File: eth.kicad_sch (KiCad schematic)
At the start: 34 parts

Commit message: add USB
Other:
- company: (none) -> M-Labs
- title: (none) -> Kirdy
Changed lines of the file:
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@@
 (kicad_sch (version 20211123) (generator eeschema)
   (paper "A3")
+  (title_block
+    (title "Kirdy")
+    (date "2022-07-03")
+    (rev "r0.1")
+    (company "M-Labs")
+    (comment 1 "Alex Wong Tat Hang")
+  )
   (junction (at 191.77 163.83) (diameter 0) (color 0 0 0 0)
   )

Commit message: complete mcu
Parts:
- gave numbers to parts that had none: 34

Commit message: first draft complete
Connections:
- net +3V3: now also C166.1, U26.9 (VDDIO)
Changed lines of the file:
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@@
     (pin "2")
+  )
+  (symbol (lib_id "power:+3V3") (at 191.77 151.13 0) (unit 1)
+    (in_bom yes) (on_board yes)
+    (property "Reference" "#PWR0161" (id 0) (at 191.77 154.94 0)
+      (effects (font (size 1.27 1.27)) hide)
+    )
+    (property "Value" "+3V3" (id 1) (at 191.77 147.32 0))
+    (property "Footprint" "" (id 2) (at 191.77 151.13 0)
+      (effects (font (size 1.27 1.27)) hide)
+    )
+    (property "Datasheet" "" (id 3) (at 191.77 151.13 0)
+      (effects (font (size 1.27 1.27)) hide)
+    )
+    (pin "1")
   )
   (symbol (lib_id "Device:R") (at 300.99 128.27 90) (unit 1)
@@
     (pin "2")
   )
+  (symbol (lib_id "power:PWR_FLAG") (at 204.47 146.05 0) (unit 1)
+    (in_bom yes) (on_board yes) (fields_autoplaced)
+    (property "Reference" "#FLG0117" (id 0) (at 204.47 144.145 0)
+      (effects (font (size 1.27 1.27)) hide)
+    )
+    (property "Value" "PWR_FLAG" (id 1) (at 204.47 140.97 0)
+      (effects (font (size 1.27 1.27)) hide)
+    )
+    (property "Footprint" "" (id 2) (at 204.47 146.05 0)
+      (effects (font (size 1.27 1.27)) hide)
+    )
+    (property "Datasheet" "~" (id 3) (at 204.47 146.05 0)
+      (effects (font (size 1.27 1.27)) hide)
+    )
+    (pin "1")
+  )
   (symbol (lib_id "Device:R") (at 66.04 130.81 90) (unit 1)

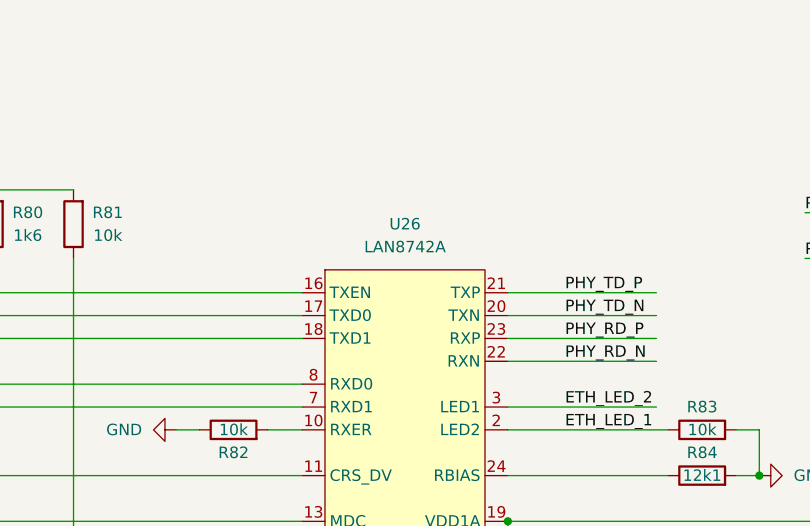
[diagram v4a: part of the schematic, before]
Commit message: Complete BOM, FP assignment
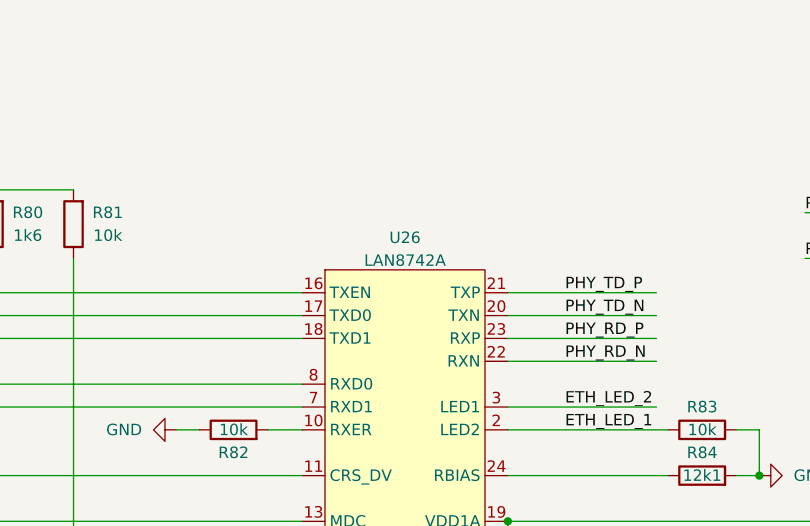
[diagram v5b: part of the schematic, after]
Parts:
- C162, C163: footprint (none) -> Capacitor_SMD:C_0603_1608Metric; MFR_PN (none) -> 0603N180J500CT; MFR_PN_ALT (none) -> CC0603JPNPO9BN180
- C164, C166, C167, C169, C170: footprint (none) -> Capacitor_SMD:C_0603_1608Metric; MFR_PN (none) -> CL10B104KB8NNWC; MFR_PN_ALT (none) -> CL10B104KB8NNNL
- C165, C168: footprint (none) -> Capacitor_SMD:C_0805_2012Metric; MFR_PN (none) -> CL21B106KOQNNNG; MFR_PN_ALT (none) -> CL21B106KOQNNNE
- C171: footprint (none) -> Capacitor_SMD:C_1206_3216Metric; MFR_PN (none) -> 12067C472KAT2A; MFR_PN_ALT (none) -> 1206B472K501NT
- FB11: footprint (none) -> Inductor_SMD:L_1210_3225Metric; MFR_PN (none) -> FBMH3225HM102NT; MFR_PN_ALT (none) -> FBMH3225HM102NTV
- J6: MFR_PN (none) -> ARJP11A-MASA-B-A-EMU2
- R73, R74, R75, R76, R85, R86, R87, R88: footprint (none) -> Resistor_SMD:R_0603_1608Metric; MFR_PN (none) -> RC0603FR-0733RL; MFR_PN_ALT (none) -> CRGCQ0603F33R
- R77, R78, R79, R81, R82, R83: footprint (none) -> Resistor_SMD:R_0603_1608Metric; MFR_PN (none) -> RNCP0603FTD10K0; MFR_PN_ALT (none) -> RMCF0603FT10K0
- R80: footprint (none) -> Resistor_SMD:R_0603_1608Metric; MFR_PN (none) -> RT0603FRE071K6L; MFR_PN_ALT (none) -> RMCF0603FT1K60
- R84: footprint (none) -> Resistor_SMD:R_0603_1608Metric; MFR_PN (none) -> RNCP0603FTD12K1; MFR_PN_ALT (none) -> CR0603-FX-1212ELF
- R89, R90: footprint (none) -> Resistor_SMD:R_0603_1608Metric; MFR_PN (none) -> WR06X2200FTL; MFR_PN_ALT (none) -> CRGCQ0603F220R
- R91: footprint (none) -> Resistor_SMD:R_0603_1608Metric; MFR_PN (none) -> RMCF0603ZT0R00; MFR_PN_ALT (none) -> CR0603-J/-000ELF
- U26: MFR_PN (none) -> LAN8742A-CZ; MFR_PN_ALT (none) -> LAN8742AI-CZ
- U27: MFR_PN (none) -> USBLC6-4SC6Y; MFR_PN_ALT (none) -> USBLC6-4SC6
- Y2: footprint (none) -> Crystal:Crystal_SMD_2016-4Pin_2.0x1.6mm; MFR_PN (none) -> FA-128 25.0000MF10Z-AC3

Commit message: routing, bom update
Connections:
- net PHY_TD_N: now also U27.4 (I/O3); no longer U27.6 (I/O4)
- net PHY_TD_P: now also U27.6 (I/O4); no longer U27.4 (I/O3)
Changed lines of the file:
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@@
     (effects (font (size 1.27 1.27)) (justify left bottom))
   )
-  (label "PHY_TD_N" (at 228.6 116.84 0)
+  (label "PHY_TD_N" (at 229.87 111.76 0)
     (effects (font (size 1.27 1.27)) (justify left bottom))
   )
@@
     (effects (font (size 1.27 1.27)) (justify left bottom))
   )
-  (label "PHY_TD_P" (at 228.6 111.76 0)
+  (label "PHY_TD_P" (at 229.87 116.84 0)
     (effects (font (size 1.27 1.27)) (justify left bottom))
   )

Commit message: more routing
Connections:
- net POE_VC+: now also J6.9 (V+); no longer J6.10 (V-)
- net POE_VC-: now also J6.10 (V-); no longer J6.9 (V+)
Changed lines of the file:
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@@
     (effects (font (size 1.27 1.27)) (justify right))
   )
-  (hierarchical_label "POE_VC-" (shape output) (at 293.37 113.03 180)
+  (hierarchical_label "POE_VC-" (shape output) (at 293.37 107.95 180)
     (effects (font (size 1.27 1.27)) (justify right))
   )
@@
     (effects (font (size 1.27 1.27)) (justify right))
   )
-  (hierarchical_label "POE_VC+" (shape output) (at 293.37 107.95 180)
+  (hierarchical_label "POE_VC+" (shape output) (at 293.37 113.03 180)
     (effects (font (size 1.27 1.27)) (justify right))
   )

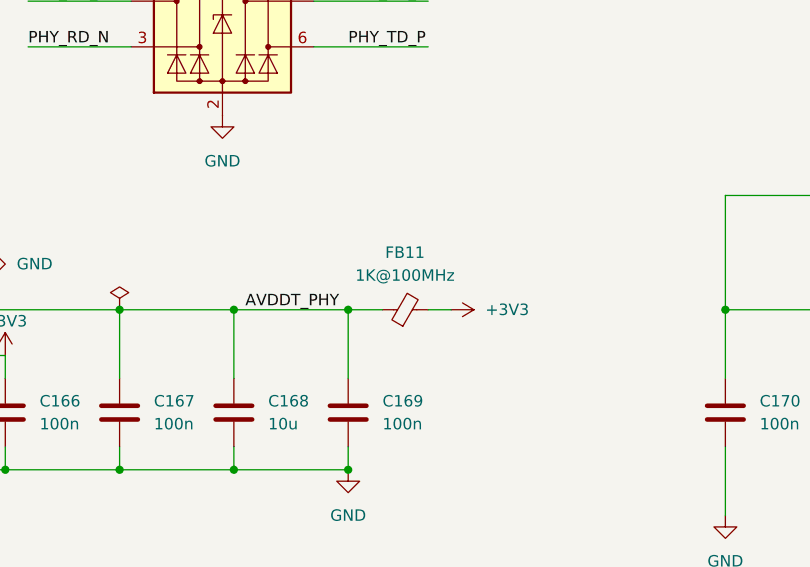
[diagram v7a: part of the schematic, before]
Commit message: add V01 production files, bug fixes
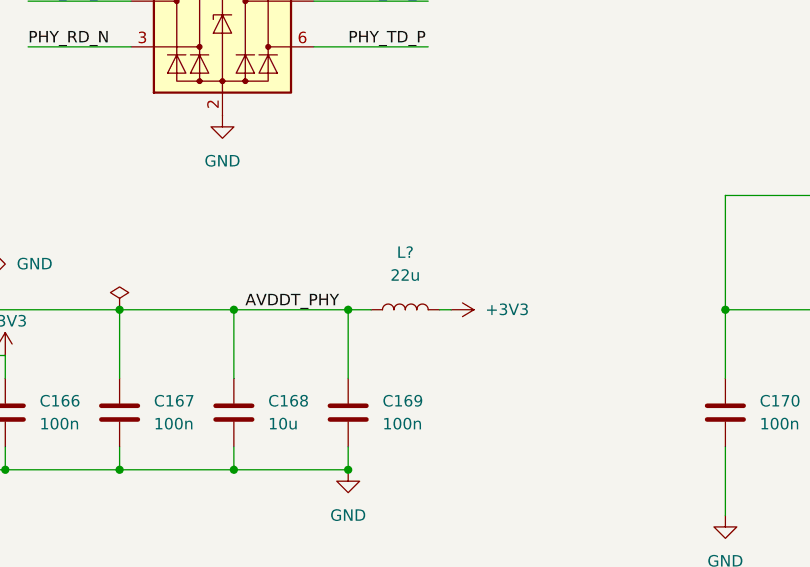
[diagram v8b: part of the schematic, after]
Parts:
- removed FB11: 1K@100MHz, Inductor_SMD:L_1210_3225Metric, symbol Device:FerriteBead_Small
- added L?: 22u, symbol Device:L
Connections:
- net +3V3: now also L?.2
- net AVDDT_PHY: now also L?.1
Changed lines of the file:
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@@
   (junction (at 363.22 168.91) (diameter 0) (color 0 0 0 0)
   )
+  (junction (at 229.87 146.05) (diameter 0) (color 0 0 0 0)
+  )
   (junction (at 77.47 130.81) (diameter 0) (color 0 0 0 0)
   )
@@
   (junction (at 95.25 140.97) (diameter 0) (color 0 0 0 0)
   )
-  (junction (at 229.87 146.05) (diameter 0) (color 0 0 0 0)
-  )
   (junction (at 217.17 163.83) (diameter 0) (color 0 0 0 0)
   )
@@
   (junction (at 161.29 146.05) (diameter 0) (color 0 0 0 0)
   )
-  (wire (pts (xy 238.76 146.05) (xy 241.3 146.05))
-    (stroke (width 0) (type default) (color 0 0 0 0))
-  )
   (wire (pts (xy 95.25 109.22) (xy 104.14 109.22))
     (stroke (width 0) (type default) (color 0 0 0 0))
@@
     (stroke (width 0) (type default) (color 0 0 0 0))
   )
-  (wire (pts (xy 229.87 146.05) (xy 233.68 146.05))
-    (stroke (width 0) (type default) (color 0 0 0 0))
-  )
   (wire (pts (xy 57.15 146.05) (xy 138.43 146.05))
     (stroke (width 0) (type default) (color 0 0 0 0))
@@
     (stroke (width 0) (type default) (color 0 0 0 0))
   )
+  (wire (pts (xy 240.03 146.05) (xy 241.3 146.05))
+    (stroke (width 0) (type default) (color 0 0 0 0))
+  )
   (wire (pts (xy 95.25 161.29) (xy 97.79 161.29))
     (stroke (width 0) (type default) (color 0 0 0 0))
@@
   )
   (wire (pts (xy 77.47 109.22) (xy 86.36 109.22))
+    (stroke (width 0) (type default) (color 0 0 0 0))
+  )
+  (wire (pts (xy 229.87 146.05) (xy 232.41 146.05))
     (stroke (width 0) (type default) (color 0 0 0 0))
   )
@@
     (pin "1")
   )
+  (symbol (lib_id "Device:L") (at 236.22 146.05 90) (unit 1)
+    (in_bom yes) (on_board yes) (fields_autoplaced)
+    (property "Reference" "L?" (id 0) (at 236.22 139.7 90))
+    (property "Value" "22u" (id 1) (at 236.22 142.24 90))
+    (property "Footprint" "" (id 2) (at 236.22 146.05 0)
+      (effects (font (size 1.27 1.27)) hide)
+    )
+    (property "Datasheet" "~" (id 3) (at 236.22 146.05 0)
+      (effects (font (size 1.27 1.27)) hide)
+    )
+    (pin "1")
+    (pin "2")
+  )
   (symbol (lib_id "Device:R") (at 104.14 113.03 180) (unit 1)
     (in_bom yes) (on_board yes)
@@
       (effects (font (size 1.27 1.27)) hide)
     )
-    (pin "1")
-    (pin "2")
-  )
-  (symbol (lib_id "Device:FerriteBead_Small") (at 236.22 146.05 90) (unit 1)
-    (in_bom yes) (on_board yes) (fields_autoplaced)
-    (property "Reference" "FB11" (id 0) (at 236.1819 139.7 90))
-    (property "Value" "1K@100MHz" (id 1) (at 236.1819 142.24 90))
-    (property "Footprint" "Inductor_SMD:L_1210_3225Metric" (id 2) (at 236.22 147.828 90)
-      (effects (font (size 1.27 1.27)) hide)
-    )
-    (property "Datasheet" "~" (id 3) (at 236.22 146.05 0)
-      (effects (font (size 1.27 1.27)) hide)
-    )
-    (property "MFR_PN" "FBMH3225HM102NT" (id 4) (at 236.22 146.05 0)
-      (effects (font (size 1.27 1.27)) hide)
-    )
-    (property "MFR_PN_ALT" "FBMH3225HM102NTV" (id 5) (at 236.22 146.05 0)
-      (effects (font (size 1.27 1.27)) hide)
-    )
